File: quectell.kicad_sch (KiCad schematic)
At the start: 0 parts

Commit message: anjir
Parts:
- added U6: FC41D, FC41D:XCVR_FC41D, symbol FC41D:FC41D
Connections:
- new net DBG_RXD_QTL: U6.25 (DBG_RXD)
- new net DBG_TXD_QTL: U6.26 (DBG_TXD)
- new net FC41D_3V3: U6.15 (VBAT)
- new net GND: U6.1 (GND), U6.16 (GND), U6.27 (GND), U6.3 (GND)
- new net I2C_SCL_QTL: U6.4 (I2C_SCL)
- new net I2C_SDA_QTL: U6.5 (I2C_SDA)
- new net LPUART1_RXD_ALT2: U6.19 (MAIN_RXD)
- new net LPUART1_TXD_ALT2: U6.20 (MAIN_TXD)

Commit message: sebelum pemeriksaan terkahir
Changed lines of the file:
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@@
 	(wire
 		(pts
-			(xy 99.06 85.09) (xy 116.84 85.09)
+			(xy 162.56 97.79) (xy 172.72 97.79)
 		)
 		(stroke
@@
 	(wire
 		(pts
-			(xy 162.56 97.79) (xy 172.72 97.79)
+			(xy 80.01 85.09) (xy 116.84 85.09)
 		)
 		(stroke
@@
 	(wire
 		(pts
-			(xy 172.72 97.79) (xy 172.72 100.33)
+			(xy 80.01 87.63) (xy 116.84 87.63)
 		)
 		(stroke
@@
 	(wire
 		(pts
-			(xy 99.06 87.63) (xy 116.84 87.63)
+			(xy 172.72 97.79) (xy 172.72 100.33)
 		)
 		(stroke
@@
 		)
 	)
+	(label "LPI2C2_SDA"
+		(at 80.01 85.09 0)
+		(fields_autoplaced yes)
+		(effects
+			(font
+				(size 1.27 1.27)
+			)
+			(justify left bottom)
+		)
+	)
 	(label "FC41D_3V3"
 		(at 213.36 46.99 180)
@@
 		(fields_autoplaced yes)
 		(effects
+			(font
+				(size 1.27 1.27)
+			)
+			(justify left bottom)
+		)
+	)
+	(label "LPI2C2_SCL"
+		(at 80.01 87.63 0)
+		(fields_autoplaced yes)
+		(effects

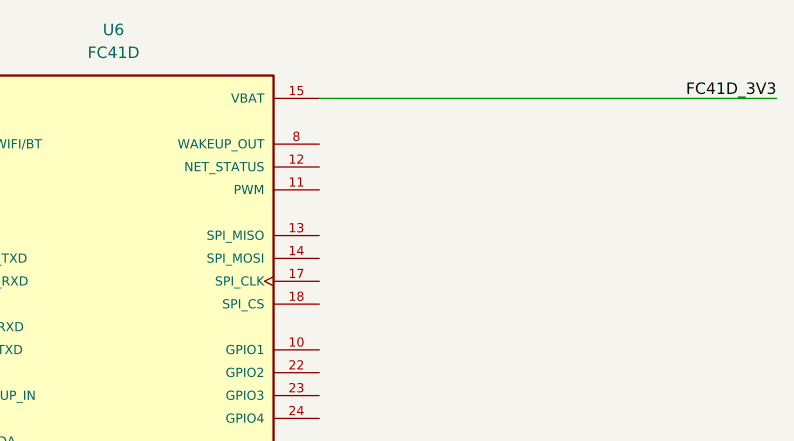
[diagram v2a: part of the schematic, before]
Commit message: Add power usb
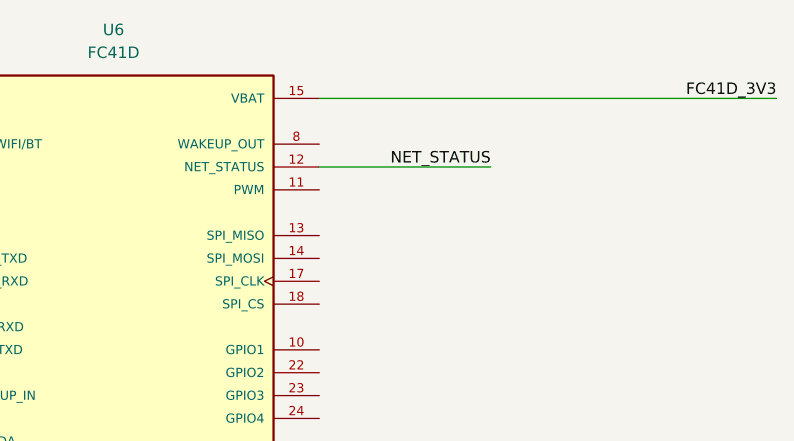
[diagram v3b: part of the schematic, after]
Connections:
- net NET_STATUS: now reaches U6.12 (NET_STATUS)
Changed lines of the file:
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@@
+	(wire
+		(pts
+			(xy 162.56 54.61) (xy 181.61 54.61)
+		)
+		(stroke
+			(width 0)
+			(type default)
+		)
+	)
 	(wire
 		(pts
@@
 		)
 	)
+	(label "NET_STATUS"
+		(at 181.61 54.61 180)
+		(fields_autoplaced yes)
+		(effects
+			(font
+				(size 1.27 1.27)
+			)
+			(justify right bottom)
+		)
+	)

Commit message: update error
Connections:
- net LPUART1_RXD_ALT2: now also U6.20 (MAIN_TXD); no longer U6.19 (MAIN_RXD)
- net LPUART1_TXD_ALT2: now also U6.19 (MAIN_RXD); no longer U6.20 (MAIN_TXD)
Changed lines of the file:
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@@
+	(wire
+		(pts
+			(xy 52.07 74.93) (xy 116.84 74.93)
+		)
+		(stroke
+			(width 0)
+			(type default)
+		)
+	)
 	(wire
 		(pts
 			(xy 52.07 64.77) (xy 116.84 64.77)
-		)
-		(stroke
-			(width 0)
-			(type default)
-		)
-	)
-	(wire
-		(pts
-			(xy 52.07 74.93) (xy 116.84 74.93)
 		)
 		(stroke
@@
 		)
 	)
-	(label "LPUART1_RXD_ALT2"
+	(label "LPUART1_TXD_ALT2"
 		(at 52.07 67.31 0)
 		(fields_autoplaced yes)
@@
 		)
 	)
+	(label "LPUART1_RXD_ALT2"
+		(at 52.07 64.77 0)
+		(fields_autoplaced yes)
+		(effects
+			(font
+				(size 1.27 1.27)
+			)
+			(justify left bottom)
+		)
+	)
 	(label "LPI2C2_SDA"
 		(at 80.01 85.09 0)
@@
 		(fields_autoplaced yes)
 		(effects
-			(font
-				(size 1.27 1.27)
-			)
-			(justify left bottom)
-		)
-	)
-	(label "LPUART1_TXD_ALT2"
-		(at 52.07 64.77 0)
-		(fields_autoplaced yes)
-		(effects

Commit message: menambah lebih dari setengah footprint
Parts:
- U6: footprint FC41D:XCVR_FC41D -> library:XCVR_FC41D
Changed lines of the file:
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@@
 			)
 		)
-		(property "Footprint" "FC41D:XCVR_FC41D"
+		(property "Footprint" "library:XCVR_FC41D"
 			(at 139.7 72.39 0)
 			(effects
@@
 				(hide yes)
 			)
+		)
+		(property "DigikeyPartNumber" ""
+			(at 139.7 72.39 0)
+			(effects
+				(font
+					(size 1.27 1.27)
+				)
+				(hide yes)
+			)

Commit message: da
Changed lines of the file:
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@@
 		)
 	)
-	(label "DBG_TXD_QTL"
+	(global_label "LPI2C2_SDA"
+		(shape input)
+		(at 80.01 85.09 0)
+		(fields_autoplaced yes)
+		(effects
+			(font
+				(size 1.27 1.27)
+			)
+			(justify left)
+		)
+		(property "Intersheetrefs" "${INTERSHEET_REFS}"
+			(at 94.1228 85.09 0)
+			(effects
+				(font
+					(size 1.27 1.27)
+				)
+				(justify left)
+				(hide yes)
+			)
+		)
+	)
+	(global_label "LPUART1_TXD_ALT2"
+		(shape input)
+		(at 52.07 67.31 0)
+		(fields_autoplaced yes)
+		(effects
+			(font
+				(size 1.27 1.27)
+			)
+			(justify left)
+		)
+		(property "Intersheetrefs" "${INTERSHEET_REFS}"
+			(at 72.8956 67.31 0)
+			(effects
+				(font
+					(size 1.27 1.27)
+				)
+				(justify left)
+				(hide yes)
+			)
+		)
+	)
+	(global_label "DBG_RXD_QTL"
+		(shape input)
+		(at 99.06 72.39 0)
+		(fields_autoplaced yes)
+		(effects
+			(font
+				(size 1.27 1.27)
+			)
+			(justify left)
+		)
+		(property "Intersheetrefs" "${INTERSHEET_REFS}"
+			(at 114.8661 72.39 0)
+			(effects
+				(font
+					(size 1.27 1.27)
+				)
+				(justify left)
+				(hide yes)
+			)
+		)
+	)
+	(global_label "LPUART2_TXD_ALT2"
+		(shape input)
+		(at 52.07 72.39 0)
+		(fields_autoplaced yes)
+		(effects
+			(font
+				(size 1.27 1.27)
+			)
+			(justify left)
+		)
+		(property "Intersheetrefs" "${INTERSHEET_REFS}"
+			(at 72.8956 72.39 0)
+			(effects
+				(font
+					(size 1.27 1.27)
+				)
+				(justify left)
+				(hide yes)
+			)
+		)
+	)
+	(global_label "I2C_SCL_QTL"
+		(shape input)
+		(at 99.06 87.63 0)
+		(fields_autoplaced yes)
+		(effects
+			(font
+				(size 1.27 1.27)
+			)
+			(justify left)
+		)
+		(property "Intersheetrefs" "${INTERSHEET_REFS}"
+			(at 113.8985 87.63 0)
+			(effects
+				(font
+					(size 1.27 1.27)
+				)
+				(justify left)
+				(hide yes)
+			)
+		)
+	)
+	(global_label "LPUART1_RXD_ALT2"
+		(shape input)
+		(at 52.07 64.77 0)
+		(fields_autoplaced yes)
+		(effects
+			(font
+				(size 1.27 1.27)
+			)
+			(justify left)
+		)
+		(property "Intersheetrefs" "${INTERSHEET_REFS}"
+			(at 73.198 64.77 0)
+			(effects
+				(font
+					(size 1.27 1.27)
+				)
+				(justify left)
+				(hide yes)
+			)
+		)
+	)
+	(global_label "NET_STATUS"
+		(shape input)
+		(at 181.61 54.61 180)
+		(fields_autoplaced yes)
+		(effects
+			(font
+				(size 1.27 1.27)
+			)
+			(justify right)
+		)
+		(property "Intersheetrefs" "${INTERSHEET_REFS}"
+			(at 167.4368 54.61 0)
+			(effects
+				(font
+					(size 1.27 1.27)
+				)
+				(justify right)
+				(hide yes)
+			)
+		)
+	)
+	(global_label "I2C_SDA_QTL"
+		(shape input)
+		(at 99.06 85.09 0)
+		(fields_autoplaced yes)
+		(effects
+			(font
+				(size 1.27 1.27)
+			)
+			(justify left)
+		)
+		(property "Intersheetrefs" "${INTERSHEET_REFS}"
+			(at 113.959 85.09 0)
+			(effects
+				(font
+					(size 1.27 1.27)
+				)
+				(justify left)
+				(hide yes)
+			)
+		)
+	)
+	(global_label "LPUART2_RXD_ALT2"
+		(shape input)
+		(at 52.07 74.93 0)
+		(fields_autoplaced yes)
+		(effects
+			(font
+				(size 1.27 1.27)
+			)
+			(justify left)
+		)
+		(property "Intersheetrefs" "${INTERSHEET_REFS}"
+			(at 73.198 74.93 0)
+			(effects
+				(font
+					(size 1.27 1.27)
+				)
+				(justify left)
+				(hide yes)
+			)
+		)
+	)
+	(global_label "FC41D_3V3"
+		(shape input)
+		(at 213.36 46.99 180)
+		(fields_autoplaced yes)
+		(effects
+			(font
+				(size 1.27 1.27)
+			)
+			(justify right)
+		)
+		(property "Intersheetrefs" "${INTERSHEET_REFS}"
+			(at 199.852 46.99 0)
+			(effects
+				(font
+					(size 1.27 1.27)
+				)
+				(justify right)
+				(hide yes)
+			)
+		)
+	)
+	(global_label "MAIN_TXD_QTL"
+		(shape input)
+		(at 99.06 64.77 0)
+		(fields_autoplaced yes)
+		(effects
+			(font
+				(size 1.27 1.27)
+			)
+			(justify left)
+		)
+		(property "Intersheetrefs" "${INTERSHEET_REFS}"
+			(at 115.229 64.77 0)
+			(effects
+				(font
+					(size 1.27 1.27)
+				)
+				(justify left)
+				(hide yes)
+			)
+		)
+	)
+	(global_label "MAIN_RXD_QTL"
+		(shape input)
+		(at 99.06 67.31 0)
+		(fields_autoplaced yes)
+		(effects
+			(font
+				(size 1.27 1.27)
+			)
+			(justify left)
+		)
+		(property "Intersheetrefs" "${INTERSHEET_REFS}"
+			(at 115.5314 67.31 0)
+			(effects
+				(font
+					(size 1.27 1.27)
+				)
+				(justify left)
+				(hide yes)
+			)
+		)
+	)
+	(global_label "DBG_TXD_QTL"
+		(shape input)
 		(at 99.06 74.93 0)
 		(fields_autoplaced yes)
@@
 				(size 1.27 1.27)
 			)
-			(justify left bottom)
-		)
-	)
-	(label "LPUART1_TXD_ALT2"
-		(at 52.07 67.31 0)
-		(fields_autoplaced yes)
-		(effects
-			(font
-				(size 1.27 1.27)
-			)
-			(justify left bottom)
-		)
-	)
-	(label "NET_STATUS"
-		(at 181.61 54.61 180)
-		(fields_autoplaced yes)
-		(effects
-			(font
-				(size 1.27 1.27)
-			)
-			(justify right bottom)
-		)
-	)
-	(label "LPUART2_TXD_ALT2"
-		(at 52.07 72.39 0)
-		(fields_autoplaced yes)
-		(effects
-			(font
-				(size 1.27 1.27)
-			)
-			(justify left bottom)
-		)
-	)
-	(label "MAIN_TXD_QTL"
-		(at 99.06 64.77 0)
-		(fields_autoplaced yes)
-		(effects
-			(font
-				(size 1.27 1.27)
-			)
-			(justify left bottom)
-		)
-	)
-	(label "LPUART1_RXD_ALT2"
-		(at 52.07 64.77 0)
-		(fields_autoplaced yes)
-		(effects
-			(font
-				(size 1.27 1.27)
-			)
-			(justify left bottom)
-		)
-	)
-	(label "LPI2C2_SDA"
-		(at 80.01 85.09 0)
-		(fields_autoplaced yes)
-		(effects
-			(font
-				(size 1.27 1.27)
-			)
-			(justify left bottom)
-		)
-	)
-	(label "FC41D_3V3"
-		(at 213.36 46.99 180)
-		(fields_autoplaced yes)
-		(effects
-			(font
-				(size 1.27 1.27)
-			)
-			(justify right bottom)
-		)
-	)
-	(label "I2C_SCL_QTL"
-		(at 99.06 87.63 0)
-		(fields_autoplaced yes)
-		(effects
-			(font
-				(size 1.27 1.27)
-			)
-			(justify left bottom)
-		)
-	)
-	(label "MAIN_RXD_QTL"
-		(at 99.06 67.31 0)
-		(fields_autoplaced yes)
-		(effects
-			(font
-				(size 1.27 1.27)
-			)
-			(justify left bottom)
-		)
-	)
-	(label "DBG_RXD_QTL"
-		(at 99.06 72.39 0)
-		(fields_autoplaced yes)
-		(effects
-			(font
-				(size 1.27 1.27)
-			)
-			(justify left bottom)
-		)
-	)
-	(label "LPUART2_RXD_ALT2"
-		(at 52.07 74.93 0)
-		(fields_autoplaced yes)
-		(effects
-			(font
-				(size 1.27 1.27)
-			)
-			(justify left bottom)
-		)
-	)
-	(label "LPI2C2_SCL"
+			(justify left)
+		)
+		(property "Intersheetrefs" "${INTERSHEET_REFS}"
+			(at 114.5637 74.93 0)
+			(effects
+				(font
+					(size 1.27 1.27)
+				)
+				(justify left)
+				(hide yes)
+			)
+		)
+	)
+	(global_label "LPI2C2_SCL"
+		(shape input)
 		(at 80.01 87.63 0)
 		(fields_autoplaced yes)
@@
 				(size 1.27 1.27)
 			)
-			(justify left bottom)
-		)
-	)
-	(label "I2C_SDA_QTL"
-		(at 99.06 85.09 0)
-		(fields_autoplaced yes)
-		(effects
-			(font
-				(size 1.27 1.27)
-			)
-			(justify left bottom)
-		)
-	)
+			(justify left)
+		)
+		(property "Intersheetrefs" "${INTERSHEET_REFS}"
+			(at 94.0623 87.63 0)
+			(effects
+				(font
+					(size 1.27 1.27)
+				)
+				(justify left)
+				(hide yes)
+			)
+		)
+	)
